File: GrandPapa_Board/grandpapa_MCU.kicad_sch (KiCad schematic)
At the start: 23 parts, among them J6 Conn_02x06, U10 MCP2515, U7 MCP2562, U8 MCP2562, U9 PIC18F26K83, Y1 12MHz

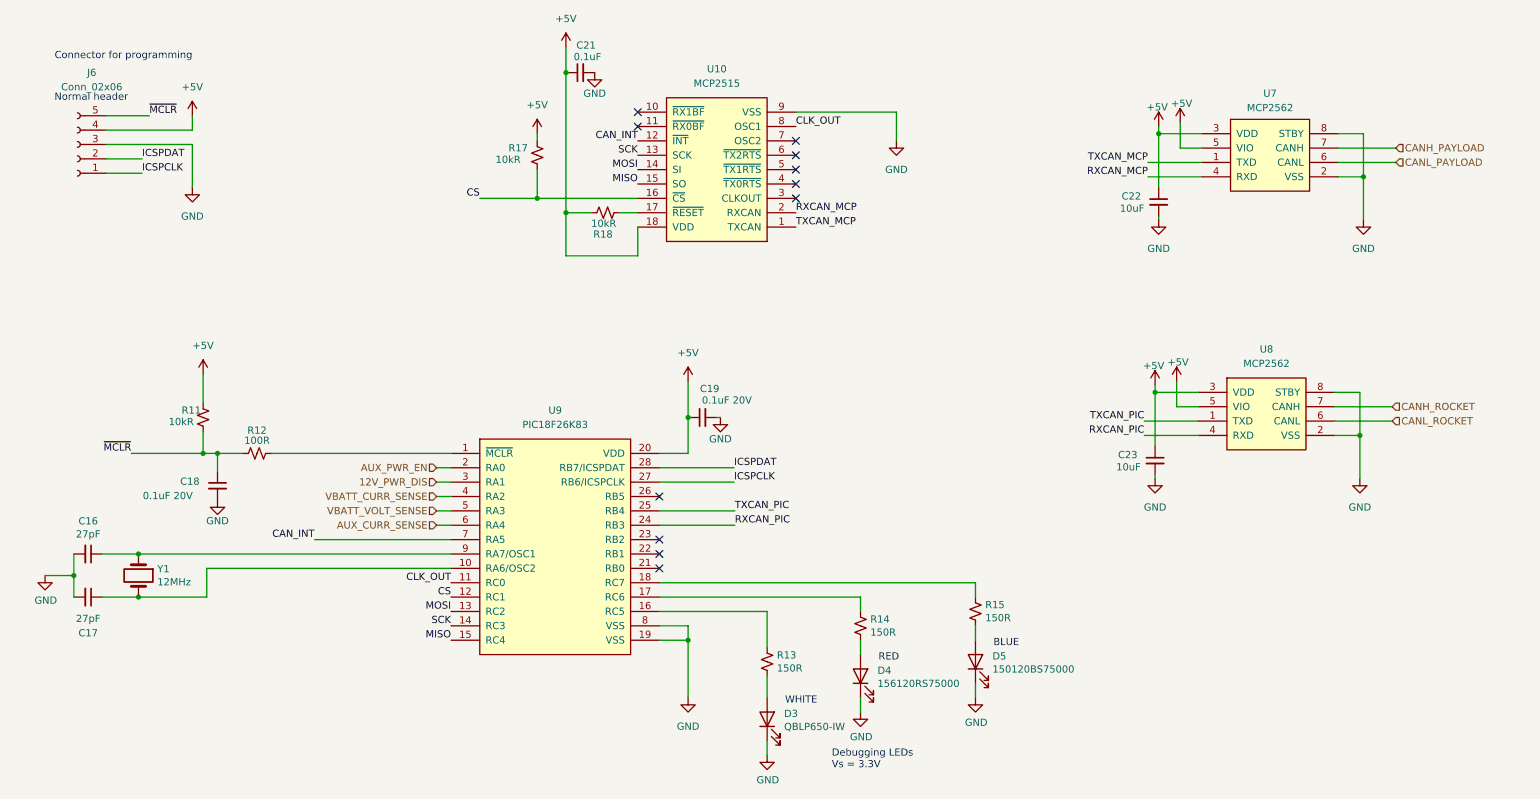
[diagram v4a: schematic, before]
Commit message: address the rest of jack's review, still need to fix grid spacing
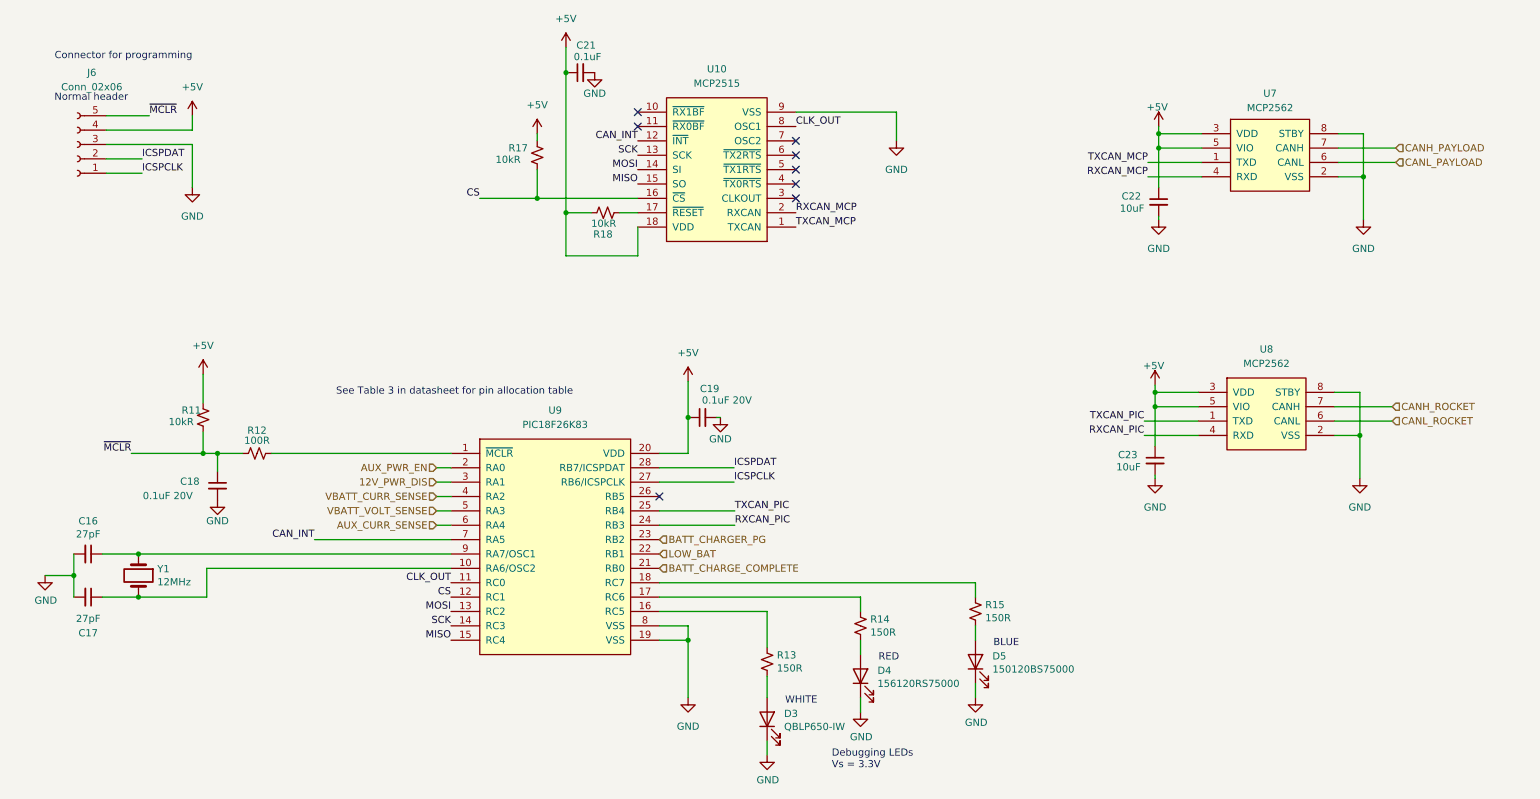
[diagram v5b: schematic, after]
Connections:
- net BATT_CHARGE_COMPLETE: now reaches U9.21 (RB0)
- net LOW_BAT: now reaches U9.22 (RB1)
- net BATT_CHARGER_PG: now reaches U9.23 (RB2)
- no-connect marks 11 -> 8
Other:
- note added: "See Table 3 in datasheet for pin allocation table"
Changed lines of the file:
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@@
   (junction (at 251.46 53.975) (diameter 0) (color 0 0 0 0)
   )
+  (junction (at 214.63 94.615) (diameter 0) (color 0 0 0 0)
+  )
   (junction (at 34.925 120.65) (diameter 0) (color 0 0 0 0)
   )
@@
   )
   (junction (at 34.925 128.27) (diameter 0) (color 0 0 0 0)
+  )
+  (junction (at 215.265 48.895) (diameter 0) (color 0 0 0 0)
   )
   (junction (at 105.41 57.785) (diameter 0) (color 0 0 0 0)
@@
   (no_connect (at 151.13 55.245))
   (no_connect (at 151.13 57.785))
-  (no_connect (at 127 123.19))
-  (no_connect (at 127 120.65))
   (no_connect (at 127 110.49))
-  (no_connect (at 127 118.11))
   (wire (pts (xy 250.825 99.695) (xy 250.825 92.075))
     (stroke (width 0) (type default) (color 0 0 0 0))
@@
     (stroke (width 0) (type default) (color 0 0 0 0))
   )
-  (wire (pts (xy 219.075 44.45) (xy 219.075 48.895))
-    (stroke (width 0) (type default) (color 0 0 0 0))
-  )
   (wire (pts (xy 29.21 43.18) (xy 36.83 43.18))
     (stroke (width 0) (type default) (color 0 0 0 0))
@@
     (stroke (width 0) (type default) (color 0 0 0 0))
   )
+  (wire (pts (xy 215.265 48.895) (xy 215.265 55.88))
+    (stroke (width 0) (type default) (color 0 0 0 0))
+  )
   (wire (pts (xy 214.63 106.68) (xy 214.63 107.315))
     (stroke (width 0) (type default) (color 0 0 0 0))
@@
     (stroke (width 0) (type default) (color 0 0 0 0))
   )
-  (wire (pts (xy 214.63 92.075) (xy 214.63 101.6))
+  (wire (pts (xy 214.63 92.075) (xy 214.63 94.615))
     (stroke (width 0) (type default) (color 0 0 0 0))
   )
@@
     (stroke (width 0) (type default) (color 0 0 0 0))
   )
-  (wire (pts (xy 222.885 48.895) (xy 219.075 48.895))
+  (wire (pts (xy 215.265 48.895) (xy 222.885 48.895))
     (stroke (width 0) (type default) (color 0 0 0 0))
   )
@@
     (stroke (width 0) (type default) (color 0 0 0 0))
   )
-  (wire (pts (xy 218.44 90.17) (xy 218.44 94.615))
-    (stroke (width 0) (type default) (color 0 0 0 0))
-  )
   (wire (pts (xy 29.21 45.72) (xy 44.45 45.72))
     (stroke (width 0) (type default) (color 0 0 0 0))
@@
     (stroke (width 0) (type default) (color 0 0 0 0))
   )
-  (wire (pts (xy 215.265 46.355) (xy 215.265 55.88))
+  (wire (pts (xy 215.265 46.355) (xy 215.265 48.895))
     (stroke (width 0) (type default) (color 0 0 0 0))
   )
@@
     (stroke (width 0) (type default) (color 0 0 0 0))
   )
-  (wire (pts (xy 222.25 94.615) (xy 218.44 94.615))
+  (wire (pts (xy 214.63 94.615) (xy 222.25 94.615))
     (stroke (width 0) (type default) (color 0 0 0 0))
   )
@@
     (stroke (width 0) (type default) (color 0 0 0 0))
   )
+  (wire (pts (xy 214.63 94.615) (xy 214.63 101.6))
+    (stroke (width 0) (type default) (color 0 0 0 0))
+  )
   (wire (pts (xy 34.925 120.65) (xy 90.17 120.65))
     (stroke (width 0) (type default) (color 0 0 0 0))
+  )
+  (text "See Table 3 in datasheet for pin allocation table\n"
+    (at 69.85 92.71 0)
+    (effects (font (size 1.27 1.27)) (justify left bottom))
   )
   (text "BLUE\n" (at 186.055 137.16 0)
@@
     (effects (font (size 1.27 1.27)) (justify right))
   )
+  (hierarchical_label "BATT_CHARGER_PG" (shape input) (at 127 118.11 0)
+    (effects (font (size 1.27 1.27)) (justify left))
+  )
   (hierarchical_label "AUX_PWR_EN" (shape input) (at 87.63 105.41 180)
     (effects (font (size 1.27 1.27)) (justify right))
@@
     (effects (font (size 1.27 1.27)) (justify right))
   )
+  (hierarchical_label "BATT_CHARGE_COMPLETE" (shape input) (at 127 123.19 0)
+    (effects (font (size 1.27 1.27)) (justify left))
+  )
   (hierarchical_label "AUX_CURR_SENSE" (shape input) (at 87.63 115.57 180)
     (effects (font (size 1.27 1.27)) (justify right))
   )
   (hierarchical_label "CANH_PAYLOAD" (shape input) (at 257.175 48.895 0)
+    (effects (font (size 1.27 1.27)) (justify left))
+  )
+  (hierarchical_label "LOW_BAT" (shape input) (at 127 120.65 0)
     (effects (font (size 1.27 1.27)) (justify left))
   )
@@
     (pin "1")
   )
-  (symbol (lib_id "power:+5V") (at 218.44 90.17 0) (unit 1)
-    (in_bom yes) (on_board yes)
-    (property "Reference" "#PWR052" (id 0) (at 218.44 93.98 0)
-      (effects (font (size 1.27 1.27)) hide)
-    )
-    (property "Value" "+5V" (id 1) (at 218.694 86.741 0))
-    (property "Footprint" "" (id 2) (at 218.44 90.17 0)
-      (effects (font (size 1.27 1.27)) hide)
-    )
-    (property "Datasheet" "" (id 3) (at 218.44 90.17 0)
-      (effects (font (size 1.27 1.27)) hide)
-    )
-    (pin "1")
-  )
   (symbol (lib_id "Device:R_Small_US") (at 117.475 60.325 90) (unit 1)
     (in_bom yes) (on_board yes)
@@
     (pin "2")
   )
-  (symbol (lib_id "power:+5V") (at 219.075 44.45 0) (unit 1)
-    (in_bom yes) (on_board yes)
-    (property "Reference" "#PWR051" (id 0) (at 219.075 48.26 0)
-      (effects (font (size 1.27 1.27)) hide)
-    )
-    (property "Value" "+5V" (id 1) (at 219.329 41.021 0))
-    (property "Footprint" "" (id 2) (at 219.075 44.45 0)
-      (effects (font (size 1.27 1.27)) hide)
-    )
-    (property "Datasheet" "" (id 3) (at 219.075 44.45 0)
-      (effects (font (size 1.27 1.27)) hide)
-    )
-    (pin "1")
-  )
   (symbol (lib_id "Device:R_Small_US") (at 182.88 130.81 0) (unit 1)

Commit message: fix disconnected pins, connect new hierarchical pins, misc layout changes
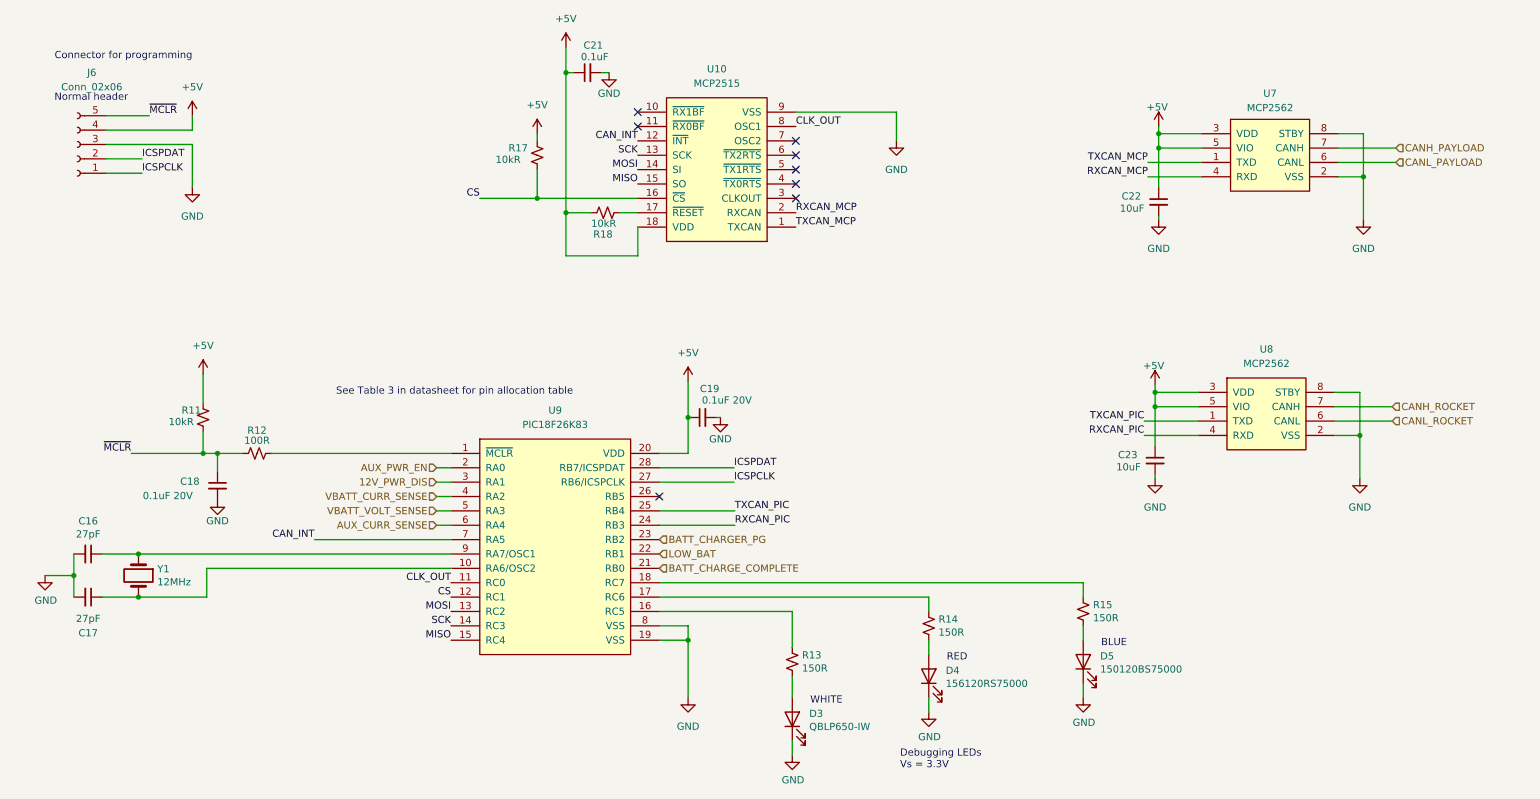
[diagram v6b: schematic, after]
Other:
- moved on the sheet: C21, D3, D4, D5, R13, R14, R15
